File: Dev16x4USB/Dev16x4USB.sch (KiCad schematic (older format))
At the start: 19 parts, among them J1 USB_B_Micro, J2 Header, J3 Header, SW1 SW_Push_DPDT, U1 LM1117-3.3, U2 ATtiny16x4-SS, U3 CH340E

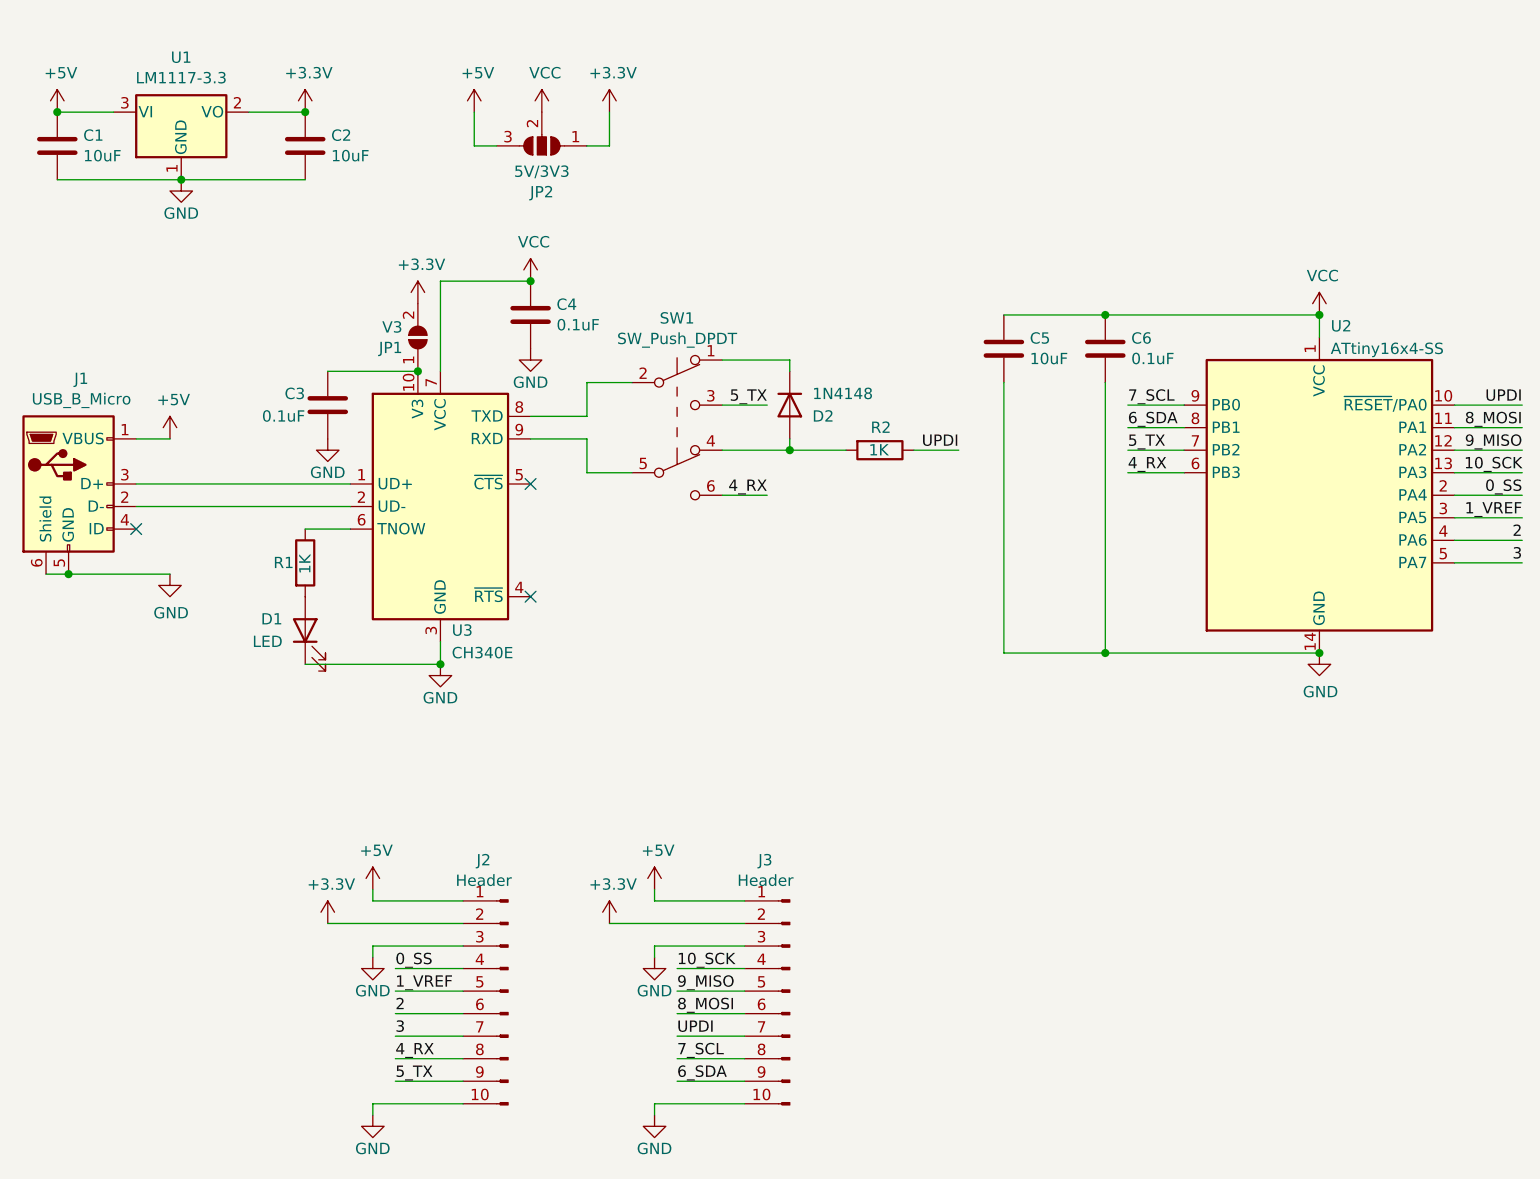
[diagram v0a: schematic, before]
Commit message: Finish v1 16x4 USB
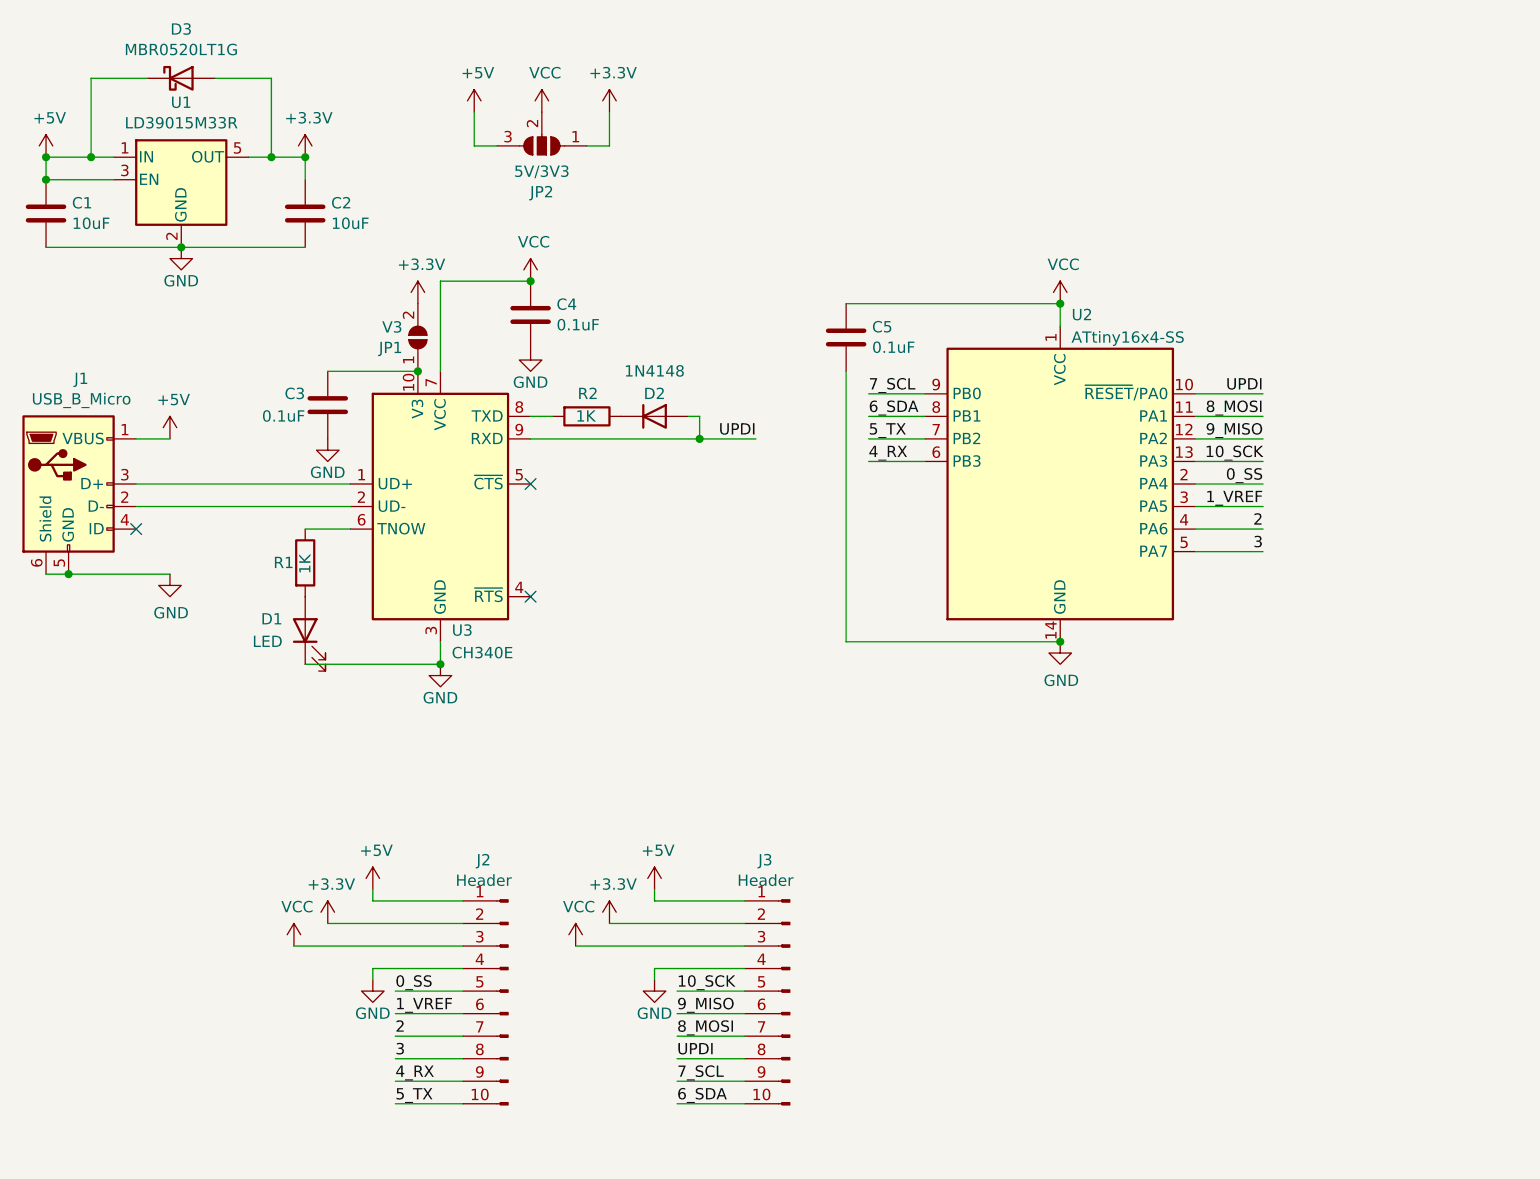
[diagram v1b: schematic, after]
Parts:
- removed C5: 10uF, Capacitor_SMD:C_0805_2012Metric, symbol Device:C
- removed SW1: SW_Push_DPDT, footprints:Wurth-452403012014, symbol Switch:SW_Push_DPDT
- removed U1: LM1117-3.3, Package_TO_SOT_SMD:SOT-223-3_TabPin2, symbol Regulator_Linear:LM1117-3.3
- added D3: MBR0520LT1G, Diode_SMD:D_SOD-123, symbol Device:D_Schottky
- added U1: LD39015M33R, Package_TO_SOT_SMD:SOT-23-5, symbol Regulator_Linear:LD39015M33R
- C1, C2, C3, C4: footprint Capacitor_SMD:C_0805_2012Metric -> Capacitor_SMD:C_0603_1608Metric
- C5: renamed from C6; footprint Capacitor_SMD:C_0805_2012Metric -> Capacitor_SMD:C_0603_1608Metric
- D2: footprint Diode_SMD:D_0805_2012Metric -> Diode_SMD:D_SOD-323
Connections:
- net +3V3: now also D3.2 (A), U1.5 (OUT)
- net +5V: now also D3.1 (K), U1.1 (IN), U1.3 (EN)
- net 0_SS: now also J2.5 (Pin_5); no longer J2.4 (Pin_4)
- net 10_SCK: now also J3.5 (Pin_5); no longer J3.4 (Pin_4)
- net 1_VREF: now also J2.6 (Pin_6); no longer J2.5 (Pin_5)
- net 2: now also J2.7 (Pin_7); no longer J2.6 (Pin_6)
- net 3: now also J2.8 (Pin_8); no longer J2.7 (Pin_7)
- net 4_RX: now also J2.9 (Pin_9); no longer J2.8 (Pin_8)
- net 5_TX: now also J2.10 (Pin_10); no longer J2.9 (Pin_9)
- net 6_SDA: now also J3.10 (Pin_10); no longer J3.9 (Pin_9)
- net 7_SCL: now also J3.9 (Pin_9); no longer J3.8 (Pin_8)
- net 8_MOSI: now also J3.7 (Pin_7); no longer J3.6 (Pin_6)
- net 9_MISO: now also J3.6 (Pin_6); no longer J3.5 (Pin_5)
- net GND: now also J2.4 (Pin_4), J3.4 (Pin_4), U1.2 (GND); no longer J2.10 (Pin_10), J2.3 (Pin_3), J3.10 (Pin_10), J3.3 (Pin_3)
- net UPDI: now also D2.2 (A), J3.8 (Pin_8), U3.9 (RXD); no longer J3.7 (Pin_7), R2.1
- net VCC: now also J2.3 (Pin_3), J3.3 (Pin_3)
- net at U3.8 (TXD): now also R2.2
- net at D2.1 (K): now also R2.1
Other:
- moved on the sheet: C1, C2, C5, D2, R2, U2
